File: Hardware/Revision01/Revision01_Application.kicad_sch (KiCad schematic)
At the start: 25 parts, among them J2 Conn_02x08_Odd_Even, J3 Conn_01x04, J4 Conn_02x08_Odd_Even, Q1 PMV32UP,215, Q2 PMV32UP,215, U2 AD7124-8BCPZ-RL7, U3 MRF89XAM9AT-I/RM, U4 ICM-45605

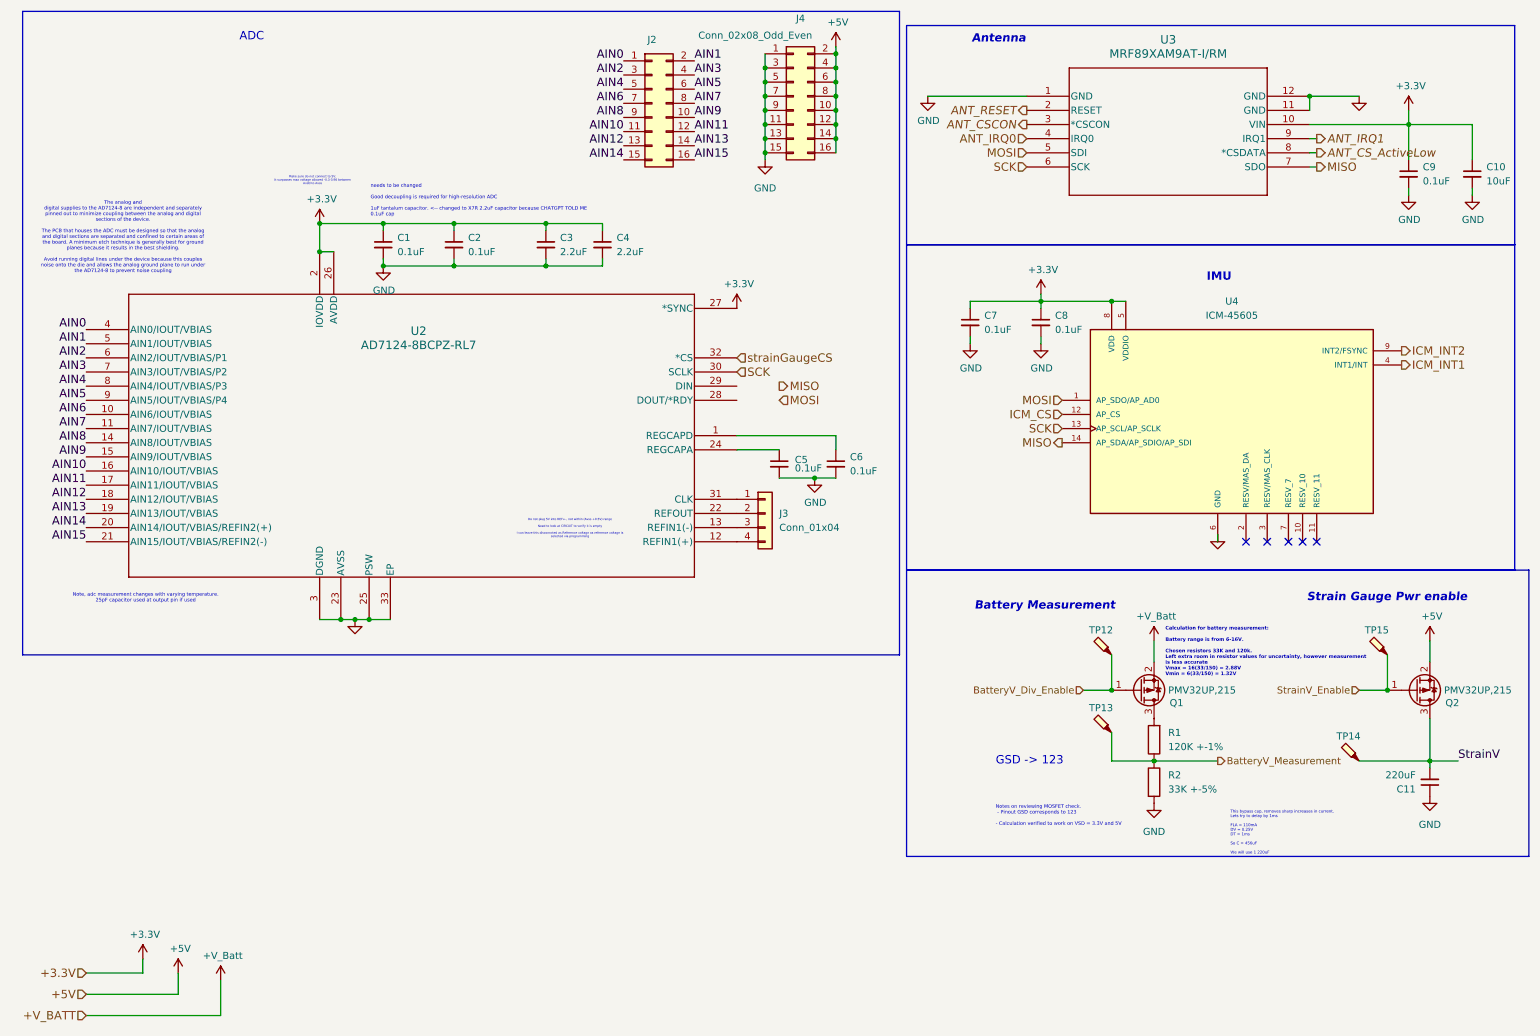
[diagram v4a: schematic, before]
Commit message: Added new LDO to fit into battery range that feeds into MCU, make sure to remove power jumper wire before connecting. Completed ERC check
Still have to put on footprints for some components when doing PCB layout
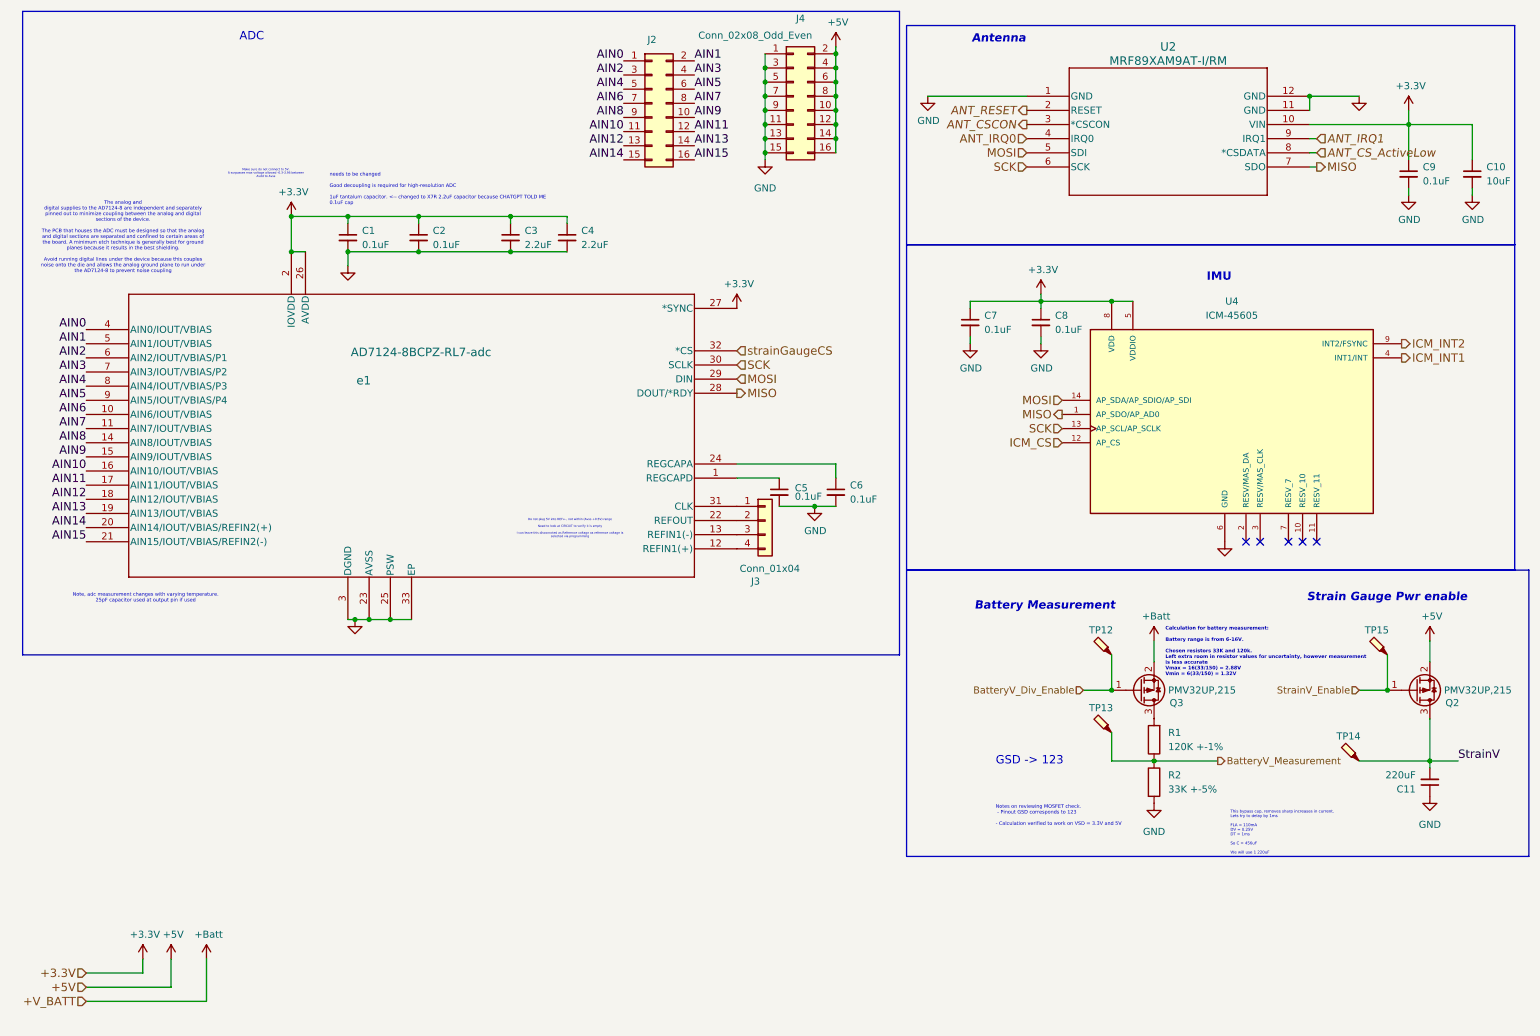
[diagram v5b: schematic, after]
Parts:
- removed Q1: PMV32UP,215, Package_TO_SOT_SMD:SOT-23, symbol Device:Q_PMOS_GSD
- removed U3: MRF89XAM9AT-I/RM, MOD_MRF89XAM9A_MCH, symbol MRF89XAM9AT-antenna:MRF89XAM9AT-I_RM
- added Q3: PMV32UP,215, Package_TO_SOT_SMD:SOT-23, symbol Transistor_FET:Q_PMOS_GSD
- added U2: MRF89XAM9AT-I/RM, MOD_MRF89XAM9A_MCH, symbol MRF89XAM9AT-antenna:MRF89XAM9AT-I_RM
- C1, C2, C5, C6, C7, C8, C9: footprint Capacitor_SMD:C_0603_1608Metric -> Capacitor_SMD:C_0805_2012Metric; Distributor link https://www.digikey.ca/en/products/detail/samsung-electro-m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 -> https://www.digikey.ca/en/products/detail/kyocera-avx/KGM21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; Manufacturer Part Number CL31B106KAHNNNE -> KGM21NR71E104KT
- C10: footprint Capacitor_SMD:C_0805_2012Metric -> Capacitor_SMD:C_1206_3216Metric; Distributor link https://www.digikey.ca/en/products/detail/kyocera-avx/18123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 -> https://www.digikey.ca/en/products/detail/samsung-electro-m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; Manufacturer KYOCERA AVX -> (none); Manufacturer Part Number 18123D106KAT2A -> KGM21NR71E104KT
- Q2: symbol Device:Q_PMOS_GSD -> Transistor_FET:Q_PMOS_GSD
- U4: symbol ICM-45605:ICM-45605 -> ICM-45605-gyroscope:ICM-45605
- e1: renamed from U2; value AD7124-8BCPZ-RL7 -> AD7124-8BCPZ-RL7-adc
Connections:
- net +3.3V: now also U2.10 (VIN)
- net ANT_CSCON: now also U2.3 (*CSCON)
- net ANT_CS_ActiveLow: now also U2.8 (*CSDATA)
- net ANT_IRQ0: now also U2.4 (IRQ0)
- net ANT_IRQ1: now also U2.9 (IRQ1)
- net ANT_RESET: now also U2.2 (RESET)
- net BatteryV_Div_Enable: now also Q3.1 (G)
- net GND: now also U2.1 (GND), U2.11 (GND), U2.12 (GND)
- net MISO: now also U4.1 (AP_SDO/AP_AD0), e1.28 (DOUT/*RDY), U2.7 (SDO); no longer U4.14 (AP_SDA/AP_SDIO/AP_SDI)
- net MOSI: now also U4.14 (AP_SDA/AP_SDIO/AP_SDI), e1.29 (DIN), U2.5 (SDI); no longer U4.1 (AP_SDO/AP_AD0)
- net SCK: now also U2.6 (SCK)
- net at R1.2: now also Q3.3 (D)
- net at C5.1: now also e1.1 (REGCAPD); no longer e1.24 (REGCAPA)
- net at C6.1: now also e1.24 (REGCAPA); no longer e1.1 (REGCAPD)
- new net +Batt: Q3.2 (S)
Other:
- moved on the sheet: C1, C2, C3, C4, C5, C6, J3

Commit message: todays review session
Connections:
- net +5V: no longer J4.10 (Pin_10), J4.12 (Pin_12), J4.14 (Pin_14), J4.16 (Pin_16), J4.2 (Pin_2), J4.4 (Pin_4), J4.6 (Pin_6), J4.8 (Pin_8)
- new net: J4.10 (Pin_10), J4.12 (Pin_12), J4.14 (Pin_14), J4.16 (Pin_16), J4.2 (Pin_2), J4.4 (Pin_4), J4.6 (Pin_6), J4.8 (Pin_8)
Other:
- note added: "Not populated Strain gauages"
- note added: "StrainV!!!"
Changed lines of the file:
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@@
+		)
+	)
+	(text "StrainV!!!"
+		(exclude_from_sim no)
+		(at 159.512 19.05 0)
+		(effects
+			(font
+				(size 0.635 0.635)
+				(color 255 7 23 1)
+			)
+			(justify left)
 		)
 	)
@@
 			(font
 				(size 0.508 0.508)
+			)
+			(justify left)
+		)
+	)
+	(text "Not populated Strain gauages"
+		(exclude_from_sim no)
+		(at 164.592 27.686 0)
+		(effects
+			(font
+				(size 0.635 0.635)
+				(color 255 7 23 1)
 			)
 			(justify left)
@@
 					(unit 1)
 				)
-			)
-		)
-	)
-	(symbol
-		(lib_id "power:+BATT")
-		(at 160.02 20.32 0)
-		(unit 1)
-		(exclude_from_sim no)
-		(in_bom yes)
-		(on_board yes)
-		(dnp no)
-		(property "Reference" "#PWR029"
-			(at 160.02 24.13 0)
-			(effects
-				(font
-					(size 1.27 1.27)
-				)
-				(hide yes)
-			)
-		)
-		(property "Value" "+5V"
-			(at 160.401 15.9258 0)
-			(effects
-				(font
-					(size 1.27 1.27)
-				)
-			)
-		)
-		(property "Footprint" ""
-			(at 160.02 20.32 0)
-			(effects
-				(font
-					(size 1.27 1.27)
-				)
-				(hide yes)
-			)
-		)
-		(property "Datasheet" ""
-			(at 160.02 20.32 0)
-			(effects
-				(font
-					(size 1.27 1.27)
-				)
-				(hide yes)
-			)
-		)
-		(property "Description" "Power symbol creates a global label with name \"+BATT\""
-			(at 160.02 20.32 0)
-			(effects
-				(font
-					(size 1.27 1.27)
-				)
-				(hide yes)
-			)
-		)
-		(pin "1"
-		)
-		(instances
-			(project "Revision01"
-				(path "/955cc99e-a129-42cf-abc7-aa99813fdb5f/00000000-0000-0000-0000-00005eb1de63"
-					(reference "#PWR029")
-					(unit 1)
-				)

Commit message: implemented feedback
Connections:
- net StrainV: now also J4.10 (Pin_10), J4.12 (Pin_12), J4.14 (Pin_14), J4.16 (Pin_16), J4.2 (Pin_2), J4.4 (Pin_4), J4.6 (Pin_6), J4.8 (Pin_8)
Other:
- note removed: "StrainV!!!"

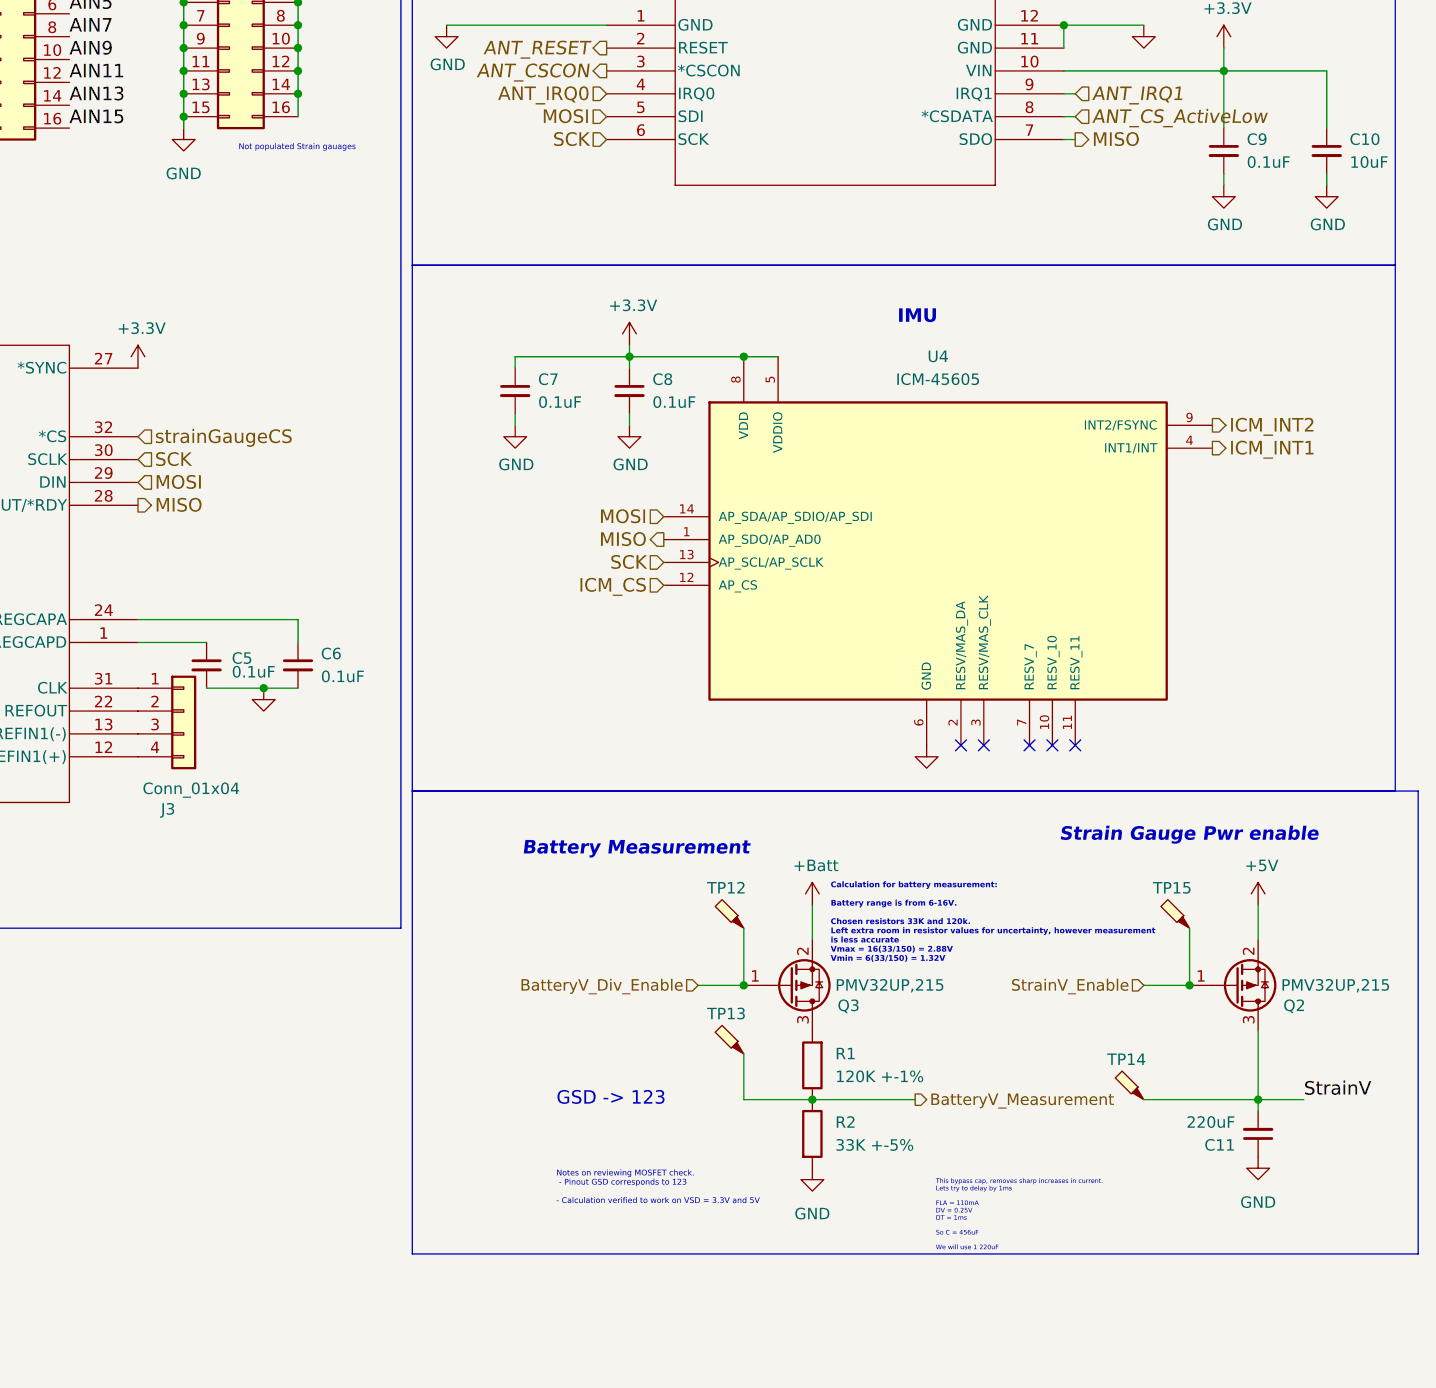
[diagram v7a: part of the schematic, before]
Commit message: some additional footprints assigned,
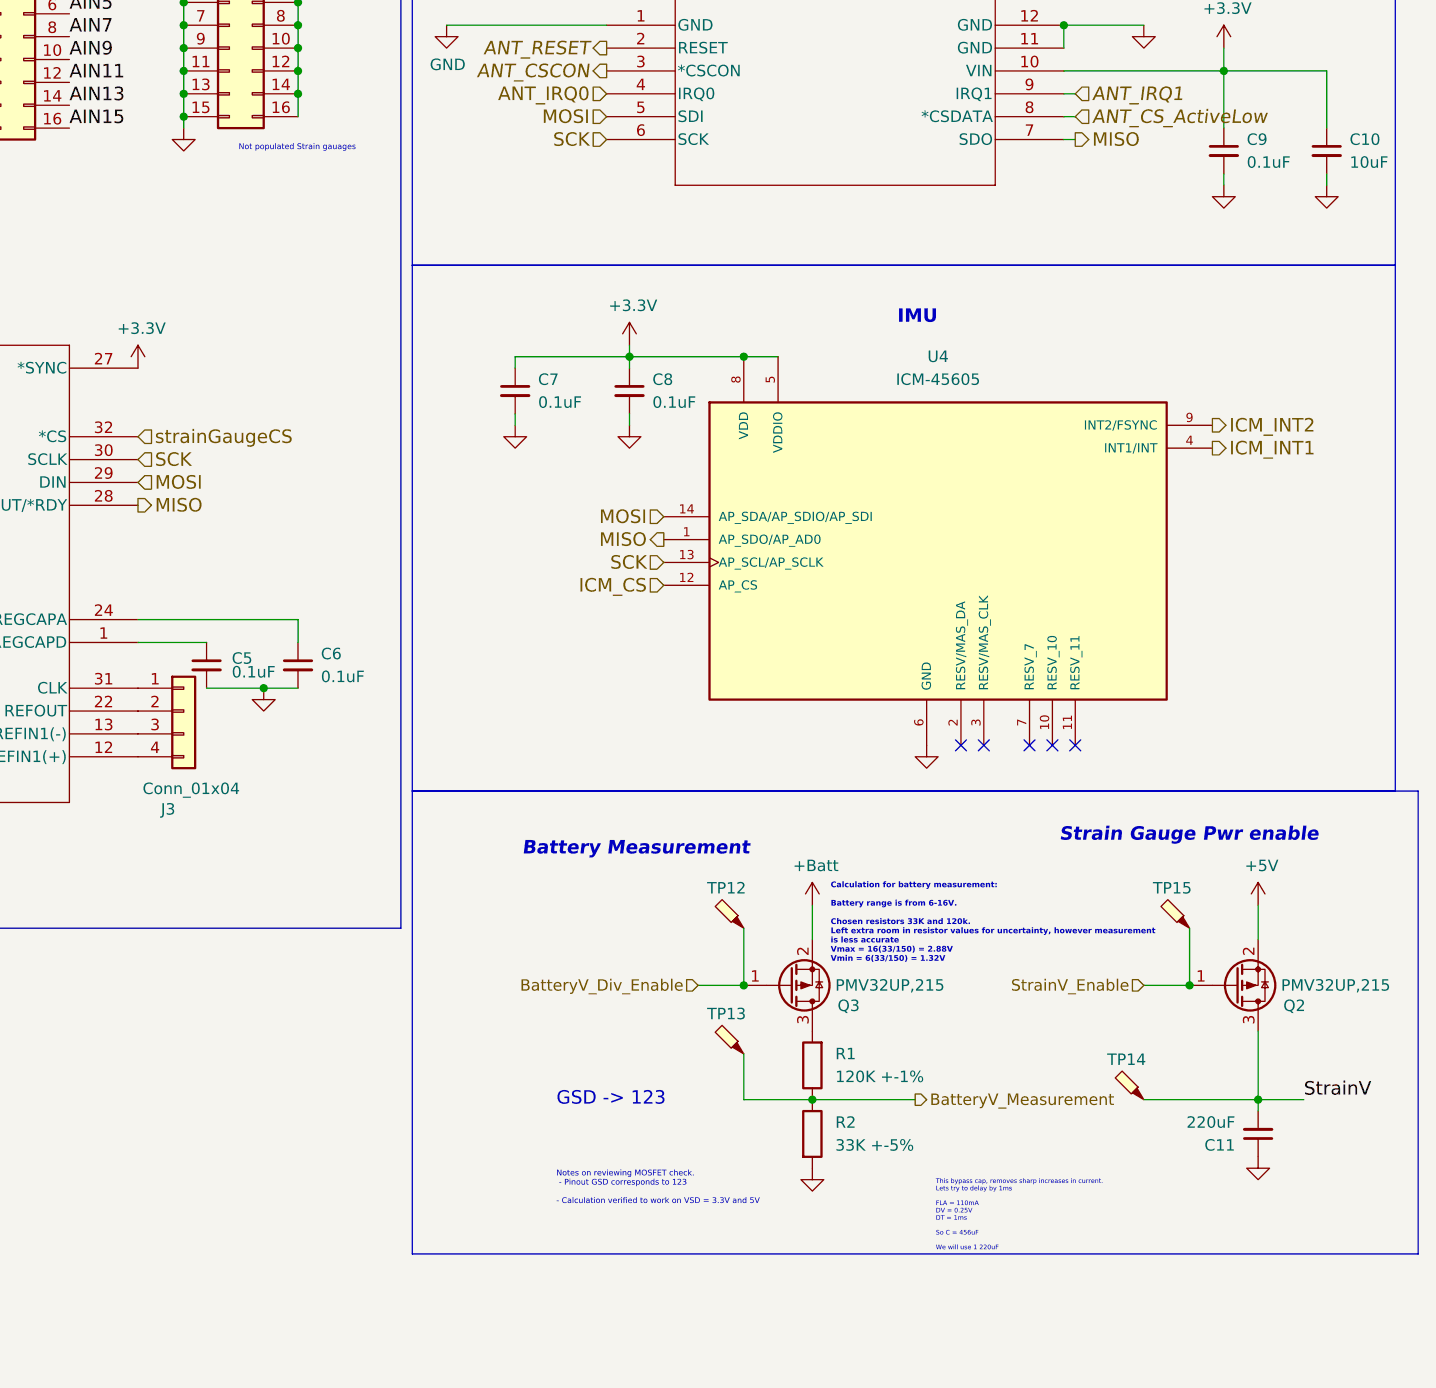
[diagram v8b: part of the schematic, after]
